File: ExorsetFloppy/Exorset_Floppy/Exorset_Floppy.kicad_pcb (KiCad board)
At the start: 2 copper layers, 160 x 100 mm, 48 parts, among them J1 BUS, SW1 SW_DIP_x08, U1 74HC21, U10 AS6C4008-55PCN, U11 AS6C4008-55PCN, U12 74HC139, U13 74HC574, U14 74HC574, U15 74HC245, U16 74HC245, U17 MXD1210, U18 74HC138, U2 GAL16V8, U3 74HC245, U4 AS6C4008-55PCN, U5 AS6C4008-55PCN, U6 AS6C4008-55PCN, U7 AS6C4008-55PCN, U8 AS6C4008-55PCN, U9 AS6C4008-55PCN

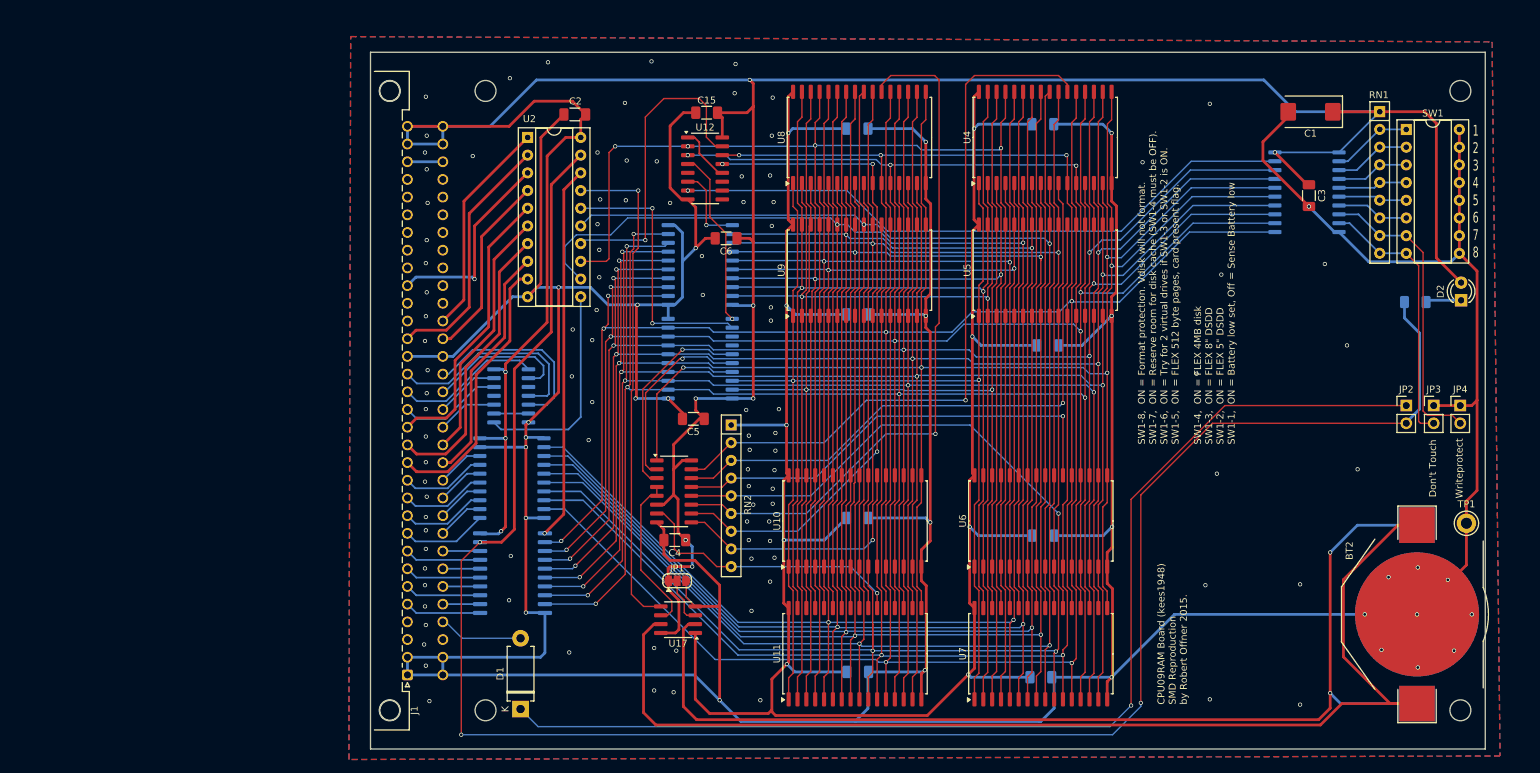
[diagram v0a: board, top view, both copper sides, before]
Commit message: Exorset Floppy added
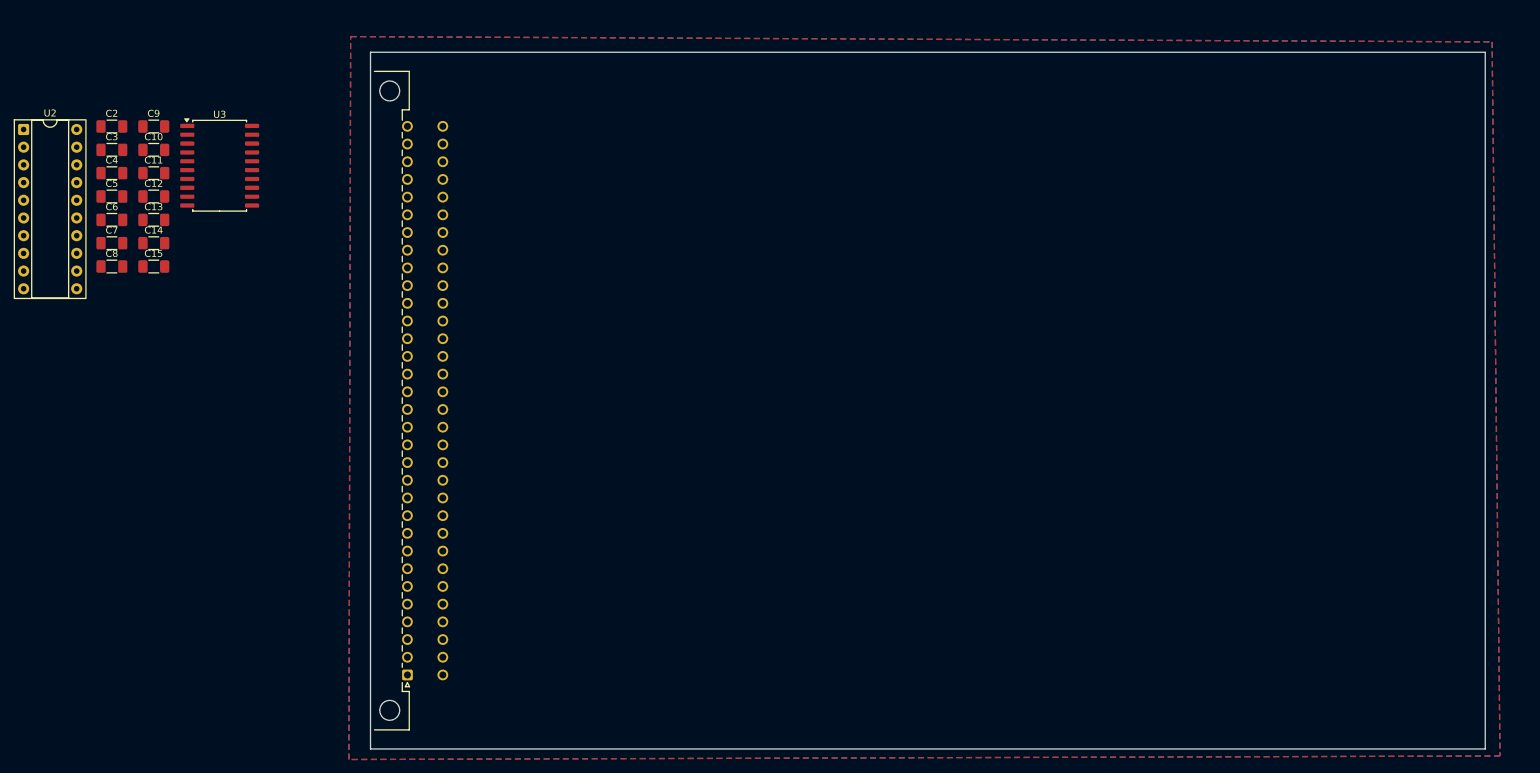
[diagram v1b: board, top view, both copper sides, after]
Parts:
- removed BT1, BT2: Battery_Cell, Battery:BatteryHolder_Keystone_3002_1x2032
- removed C1: 10u, Capacitor_Tantalum_SMD:CP_EIA-7343-31_Kemet-D_Pad2.25x2.55mm_HandSolder
- removed D1: BAT42, Diode_THT:D_DO-15_P10.16mm_Horizontal
- removed D2: RED, LED_THT:LED_D3.0mm
- removed H1: 160x100 PCB, my_own:Eurocard_160x100_19inch_holes_connector
- removed JP1: SolderJumper_3_Bridged12, Jumper:SolderJumper-3_P1.3mm_Bridged12_RoundedPad1.0x1.5mm
- removed JP2: ?, Connector_PinHeader_2.54mm:PinHeader_1x02_P2.54mm_Vertical
- removed JP3: Don't Touch, Connector_PinHeader_2.54mm:PinHeader_1x02_P2.54mm_Vertical
- removed JP4: Writeprotect, Connector_PinHeader_2.54mm:PinHeader_1x02_P2.54mm_Vertical
- removed R1: 4k7, Resistor_SMD:R_1206_3216Metric_Pad1.30x1.75mm_HandSolder
- removed RN1, RN2: 100k, Resistor_THT:R_Array_SIP9
- removed SW1: SW_DIP_x08, Package_DIP:DIP-16_W7.62mm_Socket
- removed TP1: TestPoint, TestPoint:TestPoint_Keystone_5005-5009_Compact
- removed U1: 74HC21, Package_SO:SO-14_3.9x8.65mm_P1.27mm
- removed U10, U11, U4, U5, U6, U7, U8, U9: AS6C4008-55PCN, Package_SO:SOP-32_11.305x20.495mm_P1.27mm
- removed U12: 74HC139, Package_SO:SOIC-16_3.9x9.9mm_P1.27mm
- removed U13, U14: 74HC574, Package_SO:SOP-20_7.5x12.8mm_P1.27mm
- removed U15, U16: 74HC245, Package_SO:SOP-20_7.5x12.8mm_P1.27mm
- removed U17: MXD1210, Package_SO:SOIC-8_3.9x4.9mm_P1.27mm
- removed U18: 74HC138, Package_SO:SOIC-16_3.9x9.9mm_P1.27mm
- C10, C11, C12, C13, C14, C7, C8, C9, U3: moved to F.Cu
- moved C3 171.9 mm to (22.9, 64.0), turned to 0 degrees
- moved C12 144.8 mm to (28.9, 70.7)
- moved C11 137.9 mm to (28.9, 67.4)
- moved C9 132.1 mm to (28.9, 60.7)
- moved C10 127.7 mm to (28.9, 64.0)
- moved C8 121.8 mm to (22.9, 80.8)
- moved C7 114.0 mm to (22.9, 77.4)
- moved C14 102.3 mm to (28.9, 77.4)
- moved C13 101.9 mm to (28.9, 74.1)
- moved C4 96.4 mm to (22.9, 67.4), turned to 0 degrees
- moved C5 89.4 mm to (22.9, 70.7), turned to 0 degrees
- moved C6 88.2 mm to (22.9, 74.1), turned to 0 degrees
- moved C15 82.4 mm to (28.9, 80.8), turned to 0 degrees
- moved U2 72.3 mm to (10.2, 61.1)
- moved U3 72.0 mm to (38.4, 66.3), turned to 0 degrees
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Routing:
- net GND: track 787.7 -> 0.00 mm, vias 129 -> 0
- net +5V: track 439.7 -> 0.00 mm, vias 10 -> 0
- net /ID0: track 316.2 -> 0.00 mm, vias 6 -> 0
- net /ID1: track 313.2 -> 0.00 mm, vias 6 -> 0
- net /ID2: track 311.7 -> 0.00 mm, vias 6 -> 0
- net VCC: track 311.7 -> 0.00 mm, vias 9 -> 0
- net /ID3: track 309.2 -> 0.00 mm, vias 6 -> 0
- net /ID4: track 306.7 -> 0.00 mm, vias 6 -> 0
- net /ID5: track 305.6 -> 0.00 mm, vias 6 -> 0
- net /ID6: track 304.0 -> 0.00 mm, vias 6 -> 0
- net /ID7: track 302.5 -> 0.00 mm, vias 5 -> 0
- net /IA0: track 297.2 -> 0.00 mm, vias 5 -> 0
- net /IA1: track 292.2 -> 0.00 mm, vias 5 -> 0
- net /~{DBEN}: track 283.1 -> 0.00 mm, vias 3 -> 0
- net /IA2: track 262.0 -> 0.00 mm, vias 4 -> 0
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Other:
- board text removed: "1 2 3 4 5 6 7 8"
- board text removed: "CPU09RAM Board (kees1948) SMD Reproduction by Robert Offner 2015."
- board text removed: "Hole @ 216,43/144,45"
- board text removed: "Hole @ 216,43/55,55"
- board text removed: "Hole @ 76,51/144,45"
- board text removed: "Hole @ 76,51/55,55"
- board text removed: "SW1-8, ON = Format protection. Vdisk will not format. SW1-7, ON = Reserve room for disk cache (SW1-4 must be OFF). SW1-6, ON = Try for 2 virtual drives if SW1-3 or SW1-2 is ON. SW1-5, ON = FLEX 512 byte pages, card present flag. SW1-4, ON = FLEX 4MB disk SW1-3, ON = FLEX 8{dblquote} DSDD SW1-2, ON = FLEX 5{dblquote} DSDD SW1-1, ON = Battery low set, Off = Sense Battery low"

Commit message: Exordisk first version
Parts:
- removed C10, C11, C12, C13, C14: 100n, Capacitor_SMD:C_1206_3216Metric_Pad1.33x1.80mm_HandSolder
- added C1: 10u, Capacitor_Tantalum_SMD:CP_EIA-7343-31_Kemet-D_HandSolder, B.Cu at (148.8, 56.6)
- added C16: 100u, Capacitor_Tantalum_SMD:CP_EIA-7343-31_Kemet-D_HandSolder, B.Cu at (122.7, 113.3)
- added C18: 10n, Capacitor_SMD:C_1206_3216Metric_Pad1.33x1.80mm_HandSolder, B.Cu at (162.8, 120.1)
- added C19: 8-25p, my_own:Capacitor_Trim, F.Cu at (159.5, 109.0)
- added C20: 10n, Capacitor_SMD:C_1206_3216Metric_Pad1.33x1.80mm_HandSolder, B.Cu at (174.0, 142.0)
- added C21: 1u, Capacitor_SMD:C_1206_3216Metric_Pad1.33x1.80mm_HandSolder, B.Cu at (174.0, 144.5)
- added C38: 10p, Capacitor_SMD:C_1206_3216Metric_Pad1.33x1.80mm_HandSolder, B.Cu at (146.3, 102.6)
- added C39: 56p, Capacitor_SMD:C_1206_3216Metric_Pad1.33x1.80mm_HandSolder, B.Cu at (174.0, 113.8)
- added D1: 1N4148, Diode_THT:D_5W_P10.16mm_Horizontal, F.Cu at (118.6, 110.0)
- added D2: 1N4148, Diode_THT:D_5W_P10.16mm_Horizontal, F.Cu at (136.1, 118.9)
- added D3: BAT42, Diode_THT:D_5W_P10.16mm_Horizontal, F.Cu at (172.5, 138.9)
- added J2: Floppy, Connector_PinHeader_2.54mm:PinHeader_2x17_P2.54mm_Horizontal, F.Cu at (213.1, 105.9)
- added J3: Conn_01x01, Connector_PinHeader_1.27mm:PinHeader_1x01_P1.27mm_Vertical, F.Cu at (170.9, 102.4)
- added J4: Conn_01x01, Connector_PinHeader_1.27mm:PinHeader_1x01_P1.27mm_Vertical, F.Cu at (86.4, 63.5)
- added J5: Conn_01x01, Connector_PinHeader_1.27mm:PinHeader_1x01_P1.27mm_Vertical, F.Cu at (83.8, 63.5)
- added J6: Conn_01x01, Connector_PinHeader_1.27mm:PinHeader_1x01_P1.27mm_Vertical, F.Cu at (81.3, 63.5)
- added JP1: ., Connector_PinHeader_2.54mm:PinHeader_1x03_P2.54mm_Vertical, F.Cu at (202.4, 105.9)
- added JP2: Jumper_3_Open, Jumper:SolderJumper-3_P1.3mm_Open_RoundedPad1.0x1.5mm_NumberLabels, B.Cu at (152.9, 102.6)
- added JP3: Jumper_3_Open, Jumper:SolderJumper-3_P1.3mm_Open_RoundedPad1.0x1.5mm_NumberLabels, B.Cu at (158.8, 99.1)
- added JP4: ., Connector_PinHeader_2.54mm:PinHeader_1x03_P2.54mm_Vertical, F.Cu at (196.8, 141.7)
- added JP5: ., Connector_PinHeader_2.54mm:PinHeader_1x03_P2.54mm_Vertical, F.Cu at (196.8, 145.3)
- added JP6: Jumper_3_Open, Jumper:SolderJumper-3_P1.3mm_Open_RoundedPad1.0x1.5mm_NumberLabels, B.Cu at (140.2, 102.6)
- added JP7: Jumper_3_Open, Jumper:SolderJumper-3_P1.3mm_Open_RoundedPad1.0x1.5mm_NumberLabels, B.Cu at (152.9, 110.5)
- added Q1: BC337, Package_TO_SOT_THT:TO-92L, F.Cu at (164.3, 100.3)
- added R1: 1k, Resistor_SMD:R_1206_3216Metric_Pad1.30x1.75mm_HandSolder, B.Cu at (141.2, 56.6)
- added R13: 200E, Resistor_SMD:R_1206_3216Metric_Pad1.30x1.75mm_HandSolder, B.Cu at (163.0, 97.5)
- added R14: 820E, Resistor_SMD:R_1206_3216Metric_Pad1.30x1.75mm_HandSolder, B.Cu at (163.3, 105.2)
- added R16: 1k, Resistor_SMD:R_1206_3216Metric_Pad1.30x1.75mm_HandSolder, B.Cu at (167.1, 128.8)
- added R17: 2k2, Resistor_SMD:R_1206_3216Metric_Pad1.30x1.75mm_HandSolder, B.Cu at (169.2, 119.4)
- added R18: 2k2, Resistor_SMD:R_1206_3216Metric_Pad1.30x1.75mm_HandSolder, B.Cu at (169.1, 121.7)
- added R19: 720E, Resistor_SMD:R_1206_3216Metric_Pad1.30x1.75mm_HandSolder, B.Cu at (160.3, 120.1)
- added R2: 10M, Resistor_SMD:R_1206_3216Metric_Pad1.30x1.75mm_HandSolder, B.Cu at (174.0, 147.1)
- added R3: 27k, Resistor_SMD:R_1206_3216Metric_Pad1.30x1.75mm_HandSolder, B.Cu at (132.3, 112.8)
- added R4: 47k, Resistor_SMD:R_1206_3216Metric_Pad1.30x1.75mm_HandSolder, B.Cu at (134.9, 112.8)
- added R7: 1k, Resistor_SMD:R_1206_3216Metric_Pad1.30x1.75mm_HandSolder, B.Cu at (79.8, 140.5)
- added RN2: 4k7, Resistor_THT:R_Array_SIP9, F.Cu at (209.3, 126.2)
- added U1: GAL22V10, Package_DIP:DIP-24_W7.62mm, F.Cu at (104.1, 66.0)
- added U10: GAL22V10, Package_DIP:DIP-24_W7.62mm, F.Cu at (104.1, 53.3)
- added U11: 74HCT74, Package_DIP:DIP-14_W7.62mm, F.Cu at (131.8, 64.8)
- added U12: 74HCT74, Package_DIP:DIP-14_W7.62mm, F.Cu at (176.0, 86.4)
- added U121: 74LS624, Package_DIP:DIP-14_W7.62mm, F.Cu at (152.9, 99.1)
- added U13: 74LS91, Package_DIP:DIP-14_W7.62mm, F.Cu at (198.4, 53.3)
- added U14: 74HCT74, Package_DIP:DIP-14_W7.62mm, F.Cu at (155.4, 75.7)
- added U15: 74HCT04, Package_DIP:DIP-14_W7.62mm, F.Cu at (178.6, 65.0)
- added U16: 74HCT74, Package_DIP:DIP-14_W7.62mm, F.Cu at (178.6, 75.7)
- added U17: 74HCT00, Package_DIP:DIP-14_W7.62mm, F.Cu at (131.8, 86.6)
- added U18: 74HCT74, Package_DIP:DIP-14_W7.62mm, F.Cu at (131.8, 99.1)
- added U19: 74LS76, Package_DIP:DIP-16_W7.62mm, F.Cu at (155.4, 86.6)
- added U20: 68B21, Package_DIP:DIP-40_W15.24mm, F.Cu at (125.5, 130.3)
- added U21: MC4024, Package_DIP:DIP-14_W7.62mm, F.Cu at (152.9, 99.1)
- added U22: 74LS157, Package_DIP:DIP-16_W7.62mm, F.Cu at (134.4, 75.7)
- added U221: 74LS627, Package_DIP:DIP-14_W7.62mm, F.Cu at (152.9, 99.1)
- added U23: 74LS123, Package_DIP:DIP-16_W7.62mm, F.Cu at (132.1, 118.1)
- added U24: 74HC164, Package_DIP:DIP-14_W7.62mm, F.Cu at (198.6, 65.0)
- added U27: MC4044, Package_DIP:DIP-14_W7.62mm, F.Cu at (180.8, 116.6)
- added U28: 74F163, Package_DIP:DIP-16_W7.62mm, F.Cu at (201.2, 75.7)
- added U29: 74F163, Package_DIP:DIP-16_W7.62mm, F.Cu at (201.2, 86.4)
- added U34: 6852_DIL24, Package_DIP:DIP-24_W15.24mm, F.Cu at (105.2, 100.3)
- added U4: MC8506, Package_DIP:DIP-16_W7.62mm, F.Cu at (155.4, 64.8)
- added U5: 74F163, Package_DIP:DIP-16_W7.62mm, F.Cu at (178.6, 53.3)
- added U6: 27C32, Package_DIP:DIP-24_W15.24mm, F.Cu at (105.2, 80.3)
- added U7: 74LS240, Package_DIP:DIP-20_W7.62mm, F.Cu at (154.2, 139.4)
- added U8: 74LS244, Package_DIP:DIP-20_W7.62mm, F.Cu at (154.2, 128.3)
- added U9: NE555P, Package_DIP:DIP-8_W7.62mm, F.Cu at (168.1, 139.5)
- C15, C2, C3, C5, C6: moved to B.Cu
- C7: value 100n -> 100u; footprint Capacitor_SMD:C_1206_3216Metric_Pad1.33x1.80mm_HandSolder -> Capacitor_Tantalum_SMD:CP_EIA-7343-31_Kemet-D_HandSolder; moved to B.Cu
- C8, C9: value 100n -> 100u; footprint Capacitor_SMD:C_1206_3216Metric_Pad1.33x1.80mm_HandSolder -> Capacitor_THT:CP_Radial_D10.0mm_P5.00mm
- U2: value GAL16V8 -> 74HCT74; footprint Package_DIP:DIP-20_W7.62mm_Socket -> Package_DIP:DIP-14_W7.62mm
- U3: footprint Package_SO:SOIC-20W_7.5x12.8mm_P1.27mm -> Package_DIP:DIP-20_W7.62mm
- moved C6 155.4 mm to (165.6, 135.6)
- moved C7 123.8 mm to (141.5, 113.0)
- moved U2 121.8 mm to (131.8, 53.6), turned to -90 degrees
- moved C9 121.4 mm to (138.4, 113.0)
- moved C5 111.9 mm to (115.0, 134.1)
- moved C8 108.0 mm to (125.9, 113.3), turned to 180 degrees
- moved C4 98.7 mm to (104.4, 123.0), turned to 90 degrees
- moved C3 86.1 mm to (105.1, 89.7)
- moved C2 85.1 mm to (107.2, 72.1), turned to -90 degrees
- moved U3 81.4 mm to (100.1, 119.4), turned to -90 degrees
- moved C15 46.5 mm to (69.3, 57.7)
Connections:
- C7 pad 1: VCC -> Net-(D2-A)
- C7 pad 2: GND -> Net-(U23A-Cext)
- C8 pad 1: VCC -> Net-(D1-A)
- C8 pad 2: GND -> Net-(U23B-Cext)
- C9 pad 1: VCC -> Net-(D2-A)
- C9 pad 2: GND -> Net-(U23A-Cext)
- J1 pad a27: /~{B_NMI} -> /~{NMI}
- J1 pad c26: /~{B_IRQ} -> /~{IRQ}
- U2 pad 1: /~{B_VMA} -> +5V
- U2 pad 10: GND -> +5V
- U2 pad 11: /B_A19_A13 -> /Floppy Logic/CLK_U5_15
- U2 pad 12: /IA8 -> /Floppy Logic/SHIFT_CRC
- U2 pad 13: /~{IRW} -> /Floppy Logic/RESET
- U2 pad 14: /I_0_1 -> +5V
- U2 pad 2: /B_E -> /Floppy Logic/~{EN_CRC}
- U2 pad 3: /B_Q -> /Floppy Logic/CLK_U5_15
- U2 pad 4: /~{B_RW} -> /Floppy Logic/RESET
- U2 pad 5: /BA12 -> Net-(U10-I7)
- U2 pad 6: /BA11 -> Net-(U10-I8)
- U2 pad 7: /BA10 -> GND
- U2 pad 8: /BA9 -> unconnected-(U2B-~{Q}-Pad8)
- U2 pad 9: /BA8 -> Net-(U16B-D)
- U3 pad 11: /BD0 -> /D7
- U3 pad 12: /BD1 -> /D6
- U3 pad 13: /BD2 -> /D5
- U3 pad 14: /BD3 -> /D4
- U3 pad 15: /BD4 -> /D3
- U3 pad 16: /BD5 -> /D2
- U3 pad 17: /BD6 -> /D1
- U3 pad 18: /BD7 -> /D0
- U3 pad 2: /ID7 -> /BD0
- U3 pad 3: /ID6 -> /BD1
- U3 pad 4: /ID5 -> /BD2
- U3 pad 5: /ID4 -> /BD3
- U3 pad 6: /ID3 -> /BD4
- U3 pad 7: /ID2 -> /BD5
- U3 pad 8: /ID1 -> /BD6
- U3 pad 9: /ID0 -> /BD7
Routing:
- net +5V: track 0.00 -> 937.7 mm, vias 0 -> 20
- net GND: track 0.00 -> 904.7 mm, vias 0 -> 86
- net /B_E: track 0.00 -> 195.3 mm, vias 0 -> 5
- net /Floppy Logic/~{RFF}: track 0.00 -> 154.7 mm, vias 0 -> 4
- net /Floppy Logic/RXD: track 0.00 -> 143.6 mm, vias 0 -> 4
- net /Floppy Logic/~{8x_RD_CLK}: track 0.00 -> 138.0 mm, vias 0 -> 6
- net /Floppy Logic/SLOW: track 0.00 -> 134.8 mm, vias 0 -> 3
- net /~{6820_CS}: track 0.00 -> 133.0 mm, vias 0 -> 4
- net /~{NMI}: track 0.00 -> 132.0 mm, vias 0 -> 2
- net /Floppy Logic/CRC_DATA: track 0.00 -> 124.3 mm, vias 0 -> 3
- net /BA0: track 0.00 -> 123.9 mm, vias 0 -> 3
- net /Floppy Logic/CRC-0: track 0.00 -> 123.2 mm, vias 0 -> 4
- net /~{IRQ}: track 0.00 -> 122.6 mm, vias 0 -> 1
- net /~{B_RW}: track 0.00 -> 119.2 mm, vias 0 -> 3
- net /BA1: track 0.00 -> 118.6 mm, vias 0 -> 3
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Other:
- board text added: "DS3 Pin6 Pin16"
- board text added: "MOT Pin16 Pin6"
- board text added: "Mode +5v GND"
- board text added: "Motorola Exordisk 2 for kees1948 Flex system. Use with CPUXXCMI. Robert Offner 2025"
- board text added: "U21 is 74LS624: JP2: 1-2 JP3: 2-3 JP6: 2-3 JP7: 1-2"
- board text added: "U21 is MC4024 or 74LS627: JP2: 2-3 JP3: 1-2 JP6: 1-2 JP7: 2-3"
- board text added: "Use U23A instead of U9!"
- board text added: "Use either U13 OR U24! NOT BOTH!"
